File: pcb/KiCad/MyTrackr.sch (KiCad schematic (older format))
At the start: 36 parts, among them CN1 GPS_ANTENNA, CON1 MICRO_SD, P1 CONN_OLED, P2 CONN_ICSP, P3 CONN_01X05, P4 CONN_BAT, Q1 Q_PMOS_GSD, SW1 BTN_RESET, SW2 BTN_SEL, SW3 BTN_NEXT, SW4 BTN_PREV, SW5 BTN_BACK, U0 10A45B_Module, U1 ATMEGA48_88_168_328P-32SMD, U2 GPS-NEO-6M, U3 24AA32

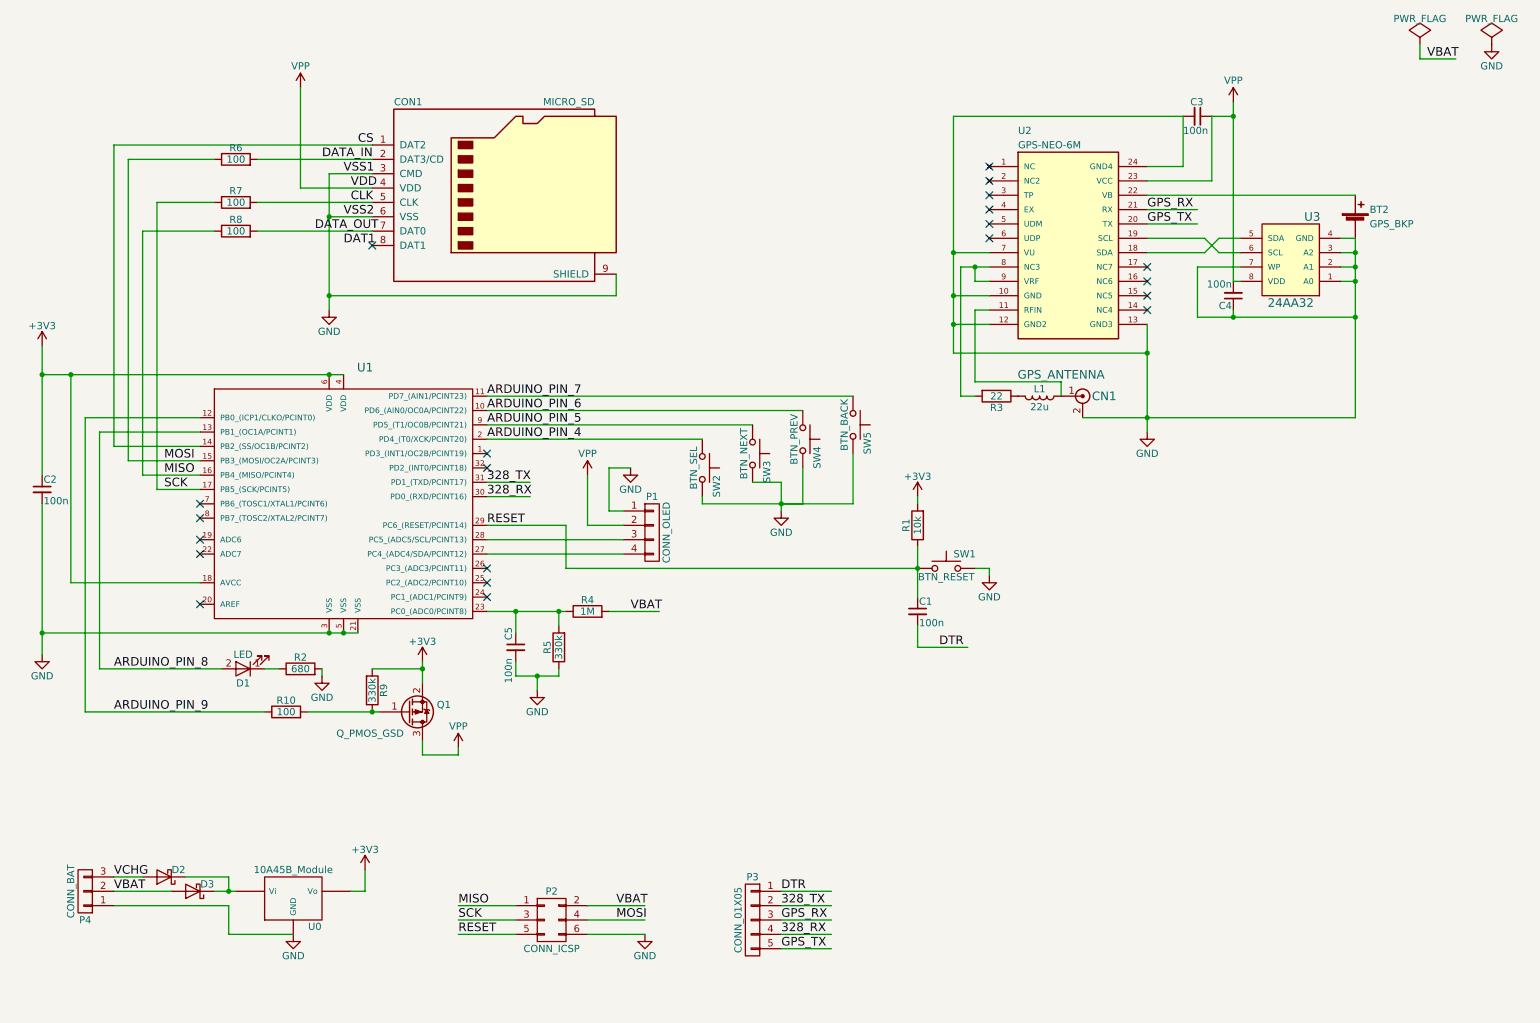
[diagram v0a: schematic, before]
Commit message: Corrections and tweaks after first prototype
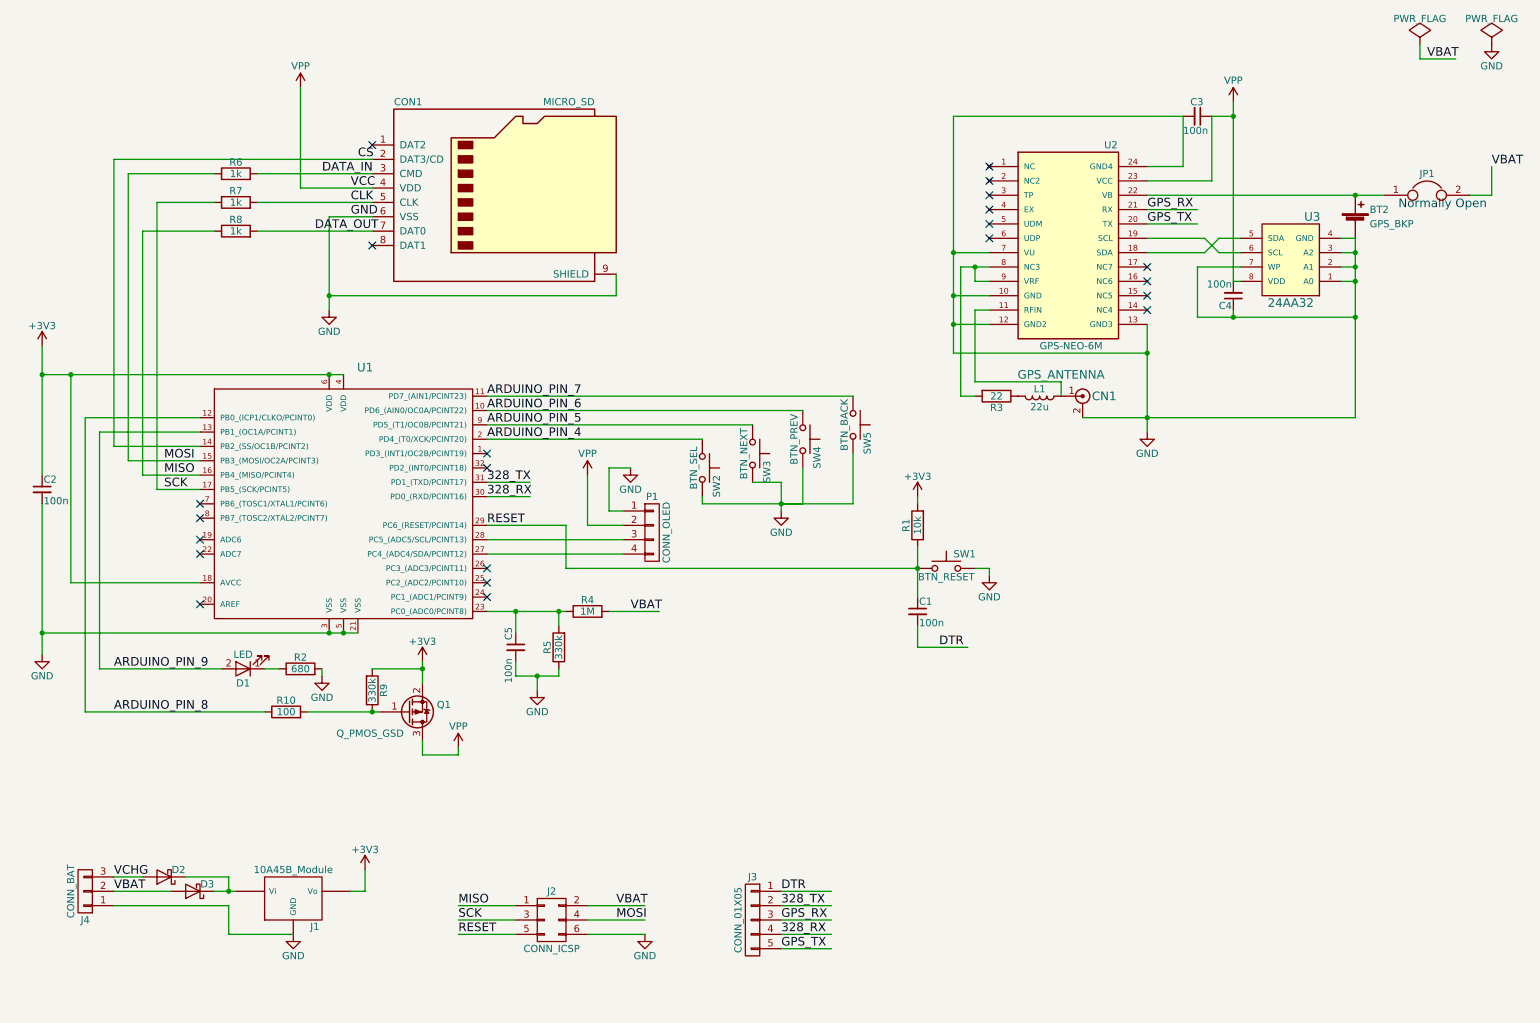
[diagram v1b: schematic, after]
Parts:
- added JP1: NO, Resistors_SMD:R_0805_HandSoldering, symbol Jumper
- R6, R7, R8: value 100 -> 1k
- U3: footprint SparkFun-Footprints:SF-SOIC-8 -> w_smd_dil:tssop-8
- renumbered U0 to J1, P2 to J2, P3 to J3, P4 to J4
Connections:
- net labels added: VCC
- net labels removed: DAT1, VDD, VSS1, VSS2
- wire segments 144 -> 145
- no-connect marks 21 -> 22
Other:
- note added: "Normally Open"
- moved on the sheet: R6

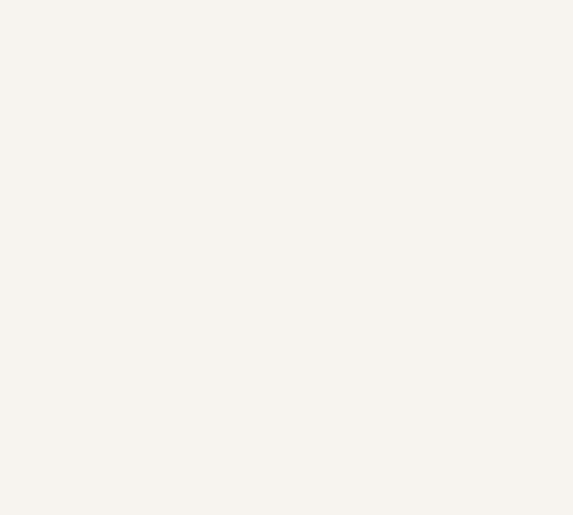
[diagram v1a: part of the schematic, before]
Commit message: Add screw holes, smooth corners and more
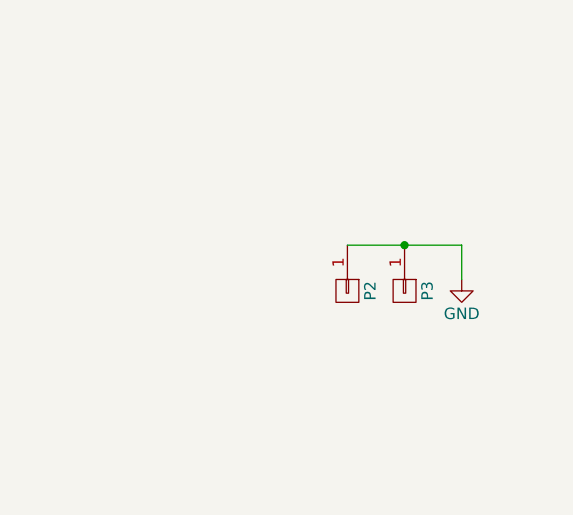
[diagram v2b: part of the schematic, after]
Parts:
- added P2, P3: CONN_01X01, Sukko:Screw_Hole_Plated_2mm, symbol CONN_01X01
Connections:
- wire segments 145 -> 147
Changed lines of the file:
@@
 Text Notes 10300 1950 0    60   ~ 0
 Normally Open
+$Comp
+L CONN_01X01 P2
+U 1 1 59B30D7B
+P 10300 6300
+F 0 "P2" H 10300 6400 50  0000 C CNN
+F 1 "CONN_01X01" V 10400 6300 50  0001 C CNN
+F 2 "Sukko:Screw_Hole_Plated_2mm" H 10300 6300 50  0001 C CNN
+F 3 "" H 10300 6300 50  0000 C CNN
+	1    10300 6300
+	0    1    1    0
+$EndComp
+$Comp
+L CONN_01X01 P3
+U 1 1 59B30E56
+P 10550 6300
+F 0 "P3" H 10550 6400 50  0000 C CNN
+F 1 "CONN_01X01" V 10650 6300 50  0001 C CNN
+F 2 "Sukko:Screw_Hole_Plated_2mm" H 10550 6300 50  0001 C CNN
+F 3 "" H 10550 6300 50  0000 C CNN
+	1    10550 6300
+	0    1    1    0
+$EndComp
+Wire Wire Line
+	10800 6100 10800 6250
+$Comp
+L GND #PWR022
+U 1 1 59B314E3
+P 10800 6250
+F 0 "#PWR022" H 10800 6000 50  0001 C CNN
+F 1 "GND" H 10800 6100 50  0000 C CNN
+F 2 "" H 10800 6250 50  0000 C CNN
+F 3 "" H 10800 6250 50  0000 C CNN
+	1    10800 6250
+	1    0    0    -1
+$EndComp
+Connection ~ 10550 6100
+Wire Wire Line
+	10300 6100 10800 6100
 $EndSCHEMATC

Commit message: Move project to KiCad 5.1.9, make all libs/footprints local
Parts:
- removed BT2: GPS_BKP, Battery_Holders:Keystone_3000_1x12mm-CoinCell, symbol Battery_Cell
- removed C1, C2, C3, C4, C5: 100n, Capacitors_SMD:C_0805_HandSoldering, symbol C_Small
- removed CON1: MICRO_SD, MicroSD GCT-MEM2055-00-190-01-A:GCT-MEM2055-00-190-01-A, symbol Micro_SD_Card
- removed D1: LED, LEDs:LED_0805, symbol LED
- removed D2, D3: D_Schottky, Diodes_SMD:SMA_Handsoldering, symbol D_Schottky
- removed J1: 10A45B_Module, Pin_Headers:Pin_Header_Straight_1x03, symbol 10A45B_Module
- removed J2: CONN_ICSP, Pin_Headers:Pin_Header_Straight_2x03, symbol CONN_02X03
- removed J3: CONN_01X05, Pin_Headers:Pin_Header_Straight_1x05, symbol CONN_01X05
- removed J4: CONN_BAT, Pin_Headers:Pin_Header_Straight_1x03, symbol CONN_01X03
- removed JP1: NO, Resistors_SMD:R_0805_HandSoldering, symbol Jumper
- removed L1: 22u, Resistors_SMD:R_0805_HandSoldering, symbol L
- removed P1: CONN_OLED, Pin_Headers:Pin_Header_Straight_1x04, symbol CONN_01X04
- removed P2, P3: CONN_01X01, Sukko:Screw_Hole_Plated_2mm, symbol CONN_01X01
- removed R1: 10k, Resistors_SMD:R_0805_HandSoldering, symbol R
- removed R10: 100, Resistors_SMD:R_0805_HandSoldering, symbol R
- removed R2: 680, Resistors_SMD:R_0805_HandSoldering, symbol R
- removed R3: 22, Resistors_SMD:R_0805_HandSoldering, symbol R
- removed R4: 1M, Resistors_SMD:R_0805_HandSoldering, symbol R
- removed R5, R9: 330k, Resistors_SMD:R_0805_HandSoldering, symbol R
- removed R6, R7, R8: 1k, Resistors_SMD:R_0805_HandSoldering, symbol R
- removed SW1: BTN_RESET, Buttons_Switches_SMD:SW_SPST_REED_CT05-XXXX-J1, symbol SW_Push
- removed SW2: BTN_SEL, MyKiCadLibs-Footprints:SW_TACT_SMD, symbol SW_Push
- removed SW3: BTN_NEXT, MyKiCadLibs-Footprints:SW_TACT_SMD, symbol SW_Push
- removed SW4: BTN_PREV, MyKiCadLibs-Footprints:SW_TACT_SMD, symbol SW_Push
- removed SW5: BTN_BACK, MyKiCadLibs-Footprints:SW_TACT_SMD, symbol SW_Push
- removed U2: GPS-NEO-6M, MOUDLE-GPS-NEO-6M_24P-16X12.2MM_:GPS24P-SMD-1.1-16X12.2MM, symbol GPS-NEO-6M
- added BT1: GPS_BKP, MyTrackr:BR1225A_KEYSTONE_1056, symbol Device:Battery_Cell
- added C1, C2, C3, C4, C5: 100n, Capacitor_SMD:C_0805_2012Metric_Pad1.18x1.45mm_HandSolder, symbol Device:C_Small
- added C6: CP1_Small, Capacitor_Tantalum_SMD:CP_EIA-7343-30_AVX-N_Pad2.25x2.55mm_HandSolder, symbol Device:CP1_Small
- added CON1: MICRO_SD, MyTrackr:GCT-MEM2055-00-190-01-A, symbol Connector:Micro_SD_Card_Det
- added D1: SS24, Diode_SMD:D_SMA, symbol Device:D_Schottky
- added H1, H2: MountingHole_Pad, MyTrackr:Screw_Hole_Plated_3mm, symbol Mechanical:MountingHole_Pad
- added J1: REGULATOR_3V3, Connector_PinHeader_2.54mm:PinHeader_1x03_P2.54mm_Vertical, symbol MyTrackr:10A45B_Module
- added J2: CONN_ICSP, Connector_PinHeader_2.54mm:PinHeader_2x03_P2.54mm_Vertical, symbol Connector_Generic:Conn_02x03_Odd_Even
- added J3: CONN_SERIAL, Connector_PinHeader_2.54mm:PinHeader_1x05_P2.54mm_Vertical, symbol Connector:Conn_01x05_Male
- added J4: CONN_BAT, Connector_PinHeader_2.54mm:PinHeader_1x03_P2.54mm_Vertical, symbol Connector:Conn_01x03_Male
- added JP1: JMP_BAT, Jumper:SolderJumper-2_P1.3mm_Open_TrianglePad1.0x1.5mm, symbol Jumper:Jumper_2_Open
- added L1: 22, Resistor_SMD:R_0805_2012Metric_Pad1.20x1.40mm_HandSolder, symbol Device:L
- added LD1: LED, LED_SMD:LED_0805_2012Metric_Pad1.15x1.40mm_HandSolder, symbol Device:LED
- added P1: CONN_OLED, Connector_PinHeader_2.54mm:PinHeader_1x04_P2.54mm_Vertical, symbol Connector:Conn_01x04_Male
- added R1: 10k, Resistor_SMD:R_0805_2012Metric_Pad1.20x1.40mm_HandSolder, symbol Device:R
- added R10: 100, Resistor_SMD:R_0805_2012Metric_Pad1.20x1.40mm_HandSolder, symbol Device:R
- added R2: 680, Resistor_SMD:R_0805_2012Metric_Pad1.20x1.40mm_HandSolder, symbol Device:R
- added R3: 22, Resistor_SMD:R_0805_2012Metric_Pad1.20x1.40mm_HandSolder, symbol Device:R
- added R4: 1M, Resistor_SMD:R_0805_2012Metric_Pad1.20x1.40mm_HandSolder, symbol Device:R
- added R5, R9: 330k, Resistor_SMD:R_0805_2012Metric_Pad1.20x1.40mm_HandSolder, symbol Device:R
- added R6, R7, R8: 1k, Resistor_SMD:R_0805_2012Metric_Pad1.20x1.40mm_HandSolder, symbol Device:R
- added SW1: BTN_RESET, Button_Switch_SMD:SW_SPST_REED_CT05-XXXX-J1, symbol Switch:SW_Push
- added SW2: BTN_SEL, Button_Switch_SMD:SW_SPST_EVPBF, symbol Switch:SW_Push
- added SW3: BTN_NEXT, Button_Switch_SMD:SW_SPST_EVPBF, symbol Switch:SW_Push
- added SW4: BTN_PREV, Button_Switch_SMD:SW_SPST_EVPBF, symbol Switch:SW_Push
- added SW5: BTN_BACK, Button_Switch_SMD:SW_SPST_EVPBF, symbol Switch:SW_Push
- added U2: GPS-NEO-6M, MyTrackr:GPS24P-SMD-1.1-16X12.2MM, symbol MOUDLE-GPS-NEO-6M_24P-16X12.2MM_:MOUDLE-GPS-NEO-6M(24P-16X12.2MM)
- added V0: OSHW_LOGO, Symbol:OSHW-Logo_5.7x6mm_Copper, symbol void:Void
- CN1: footprint MyKiCadLibs-Footprints:CONN-RF-UFL -> MyTrackr:CONN-RF-UFL; symbol COAX -> MyTrackr-rescue:COAX
- Q1: footprint TO_SOT_Packages_SMD:SOT-23_Handsoldering -> Package_TO_SOT_SMD:SOT-23; symbol Q_PMOS_GSD -> MyTrackr-rescue:Q_PMOS_GSD
- U1: footprint Housings_QFP:LQFP-32_7x7mm_Pitch0.8mm -> Package_QFP:TQFP-32_7x7mm_P0.8mm; symbol ATMEGA48_88_168_328P-32SMD -> MyTrackr-rescue:ATMEGA48_88_168_328P-32SMD
- U3: symbol 24AA32 -> MyTrackr-rescue:24AA32
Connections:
- net labels added: CARD_DETECT
- wire segments 147 -> 186
- no-connect marks 22 -> 19
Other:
- note added: "IDEAL: 200 mA, 2.7 kohm @100Mhz\n(Thanks astrobeed)"
- note added: "Short to use main battery\nfor GPS backup as well"
- note removed: "Normally Open"

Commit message: Remove old cruft
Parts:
- removed CN1: GPS_ANTENNA, MyTrackr:CONN-RF-UFL, symbol MyTrackr-rescue:COAX
- removed Q1: Q_PMOS_GSD, Package_TO_SOT_SMD:SOT-23, symbol MyTrackr-rescue:Q_PMOS_GSD
- removed U1: ATMEGA48_88_168_328P-32SMD, Package_QFP:TQFP-32_7x7mm_P0.8mm, symbol MyTrackr-rescue:ATMEGA48_88_168_328P-32SMD
- removed U3: 24AA32, w_smd_dil:tssop-8, symbol MyTrackr-rescue:24AA32
- added CN1: GPS_ANTENNA, MyTrackr:CONN-RF-UFL, symbol Connector:Conn_Coaxial
- added Q1: Q_PMOS_GSD, Package_TO_SOT_SMD:SOT-23, symbol Device:Q_PMOS_GSD
- added U1: ATMEGA328PA, Package_QFP:TQFP-32_7x7mm_P0.8mm, symbol atmega328:ATMEGA48_88_168_328P-32SMD
- added U3: 24AA32, w_smd_dil:tssop-8, symbol 24aa32:24AA32
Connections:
- net +3V3: now also Q1.2 (S), U1.18 (AVCC), U1.4 (VDD), U1.6 (VDD)
- net 328_RX: now also U1.30 (PD0_(RXD/PCINT16))
- net 328_TX: now also U1.31 (PD1_(TXD/PCINT17))
- net ARDUINO_PIN_4: now also U1.2 (PD4_(T0/XCK/PCINT20))
- net ARDUINO_PIN_5: now also U1.9 (PD5_(T1/OC0B/PCINT21))
- net ARDUINO_PIN_6: now also U1.10 (PD6_(AIN0/OC0A/PCINT22))
- net ARDUINO_PIN_7: now also U1.11 (PD7_(AIN1/PCINT23))
- net ARDUINO_PIN_8: now also U1.12 (PB0_(ICP1/CLKO/PCINT0))
- net ARDUINO_PIN_9: now also U1.13 (PB1_(OC1A/PCINT1))
- net CARD_DETECT: now also U1.32 (PD2_(INT0/PCINT18))
- net CS: now also U1.14 (PB2_(SS/OC1B/PCINT2))
- net GND: now also CN1.2 (Ext), U1.3 (VSS), U3.1 (A0), U3.2 (A1), U3.3 (A2), U3.4 (GND), U3.7 (WP)
- net MISO: now also U1.16 (PB4_(MISO/PCINT4))
- net MOSI: now also U1.15 (PB3_(MOSI/OC2A/PCINT3))
- net RESET: now also U1.29 (PC6_(RESET/PCINT14))
- net SCK: now also U1.17 (PB5_(SCK/PCINT5))
- net VPP: now also Q1.3 (D), U3.8 (VDD)
- net at L1.1, U2.11 (RFIN): now also CN1.1 (In)
- net at U2.18 (SDA): now also U3.5 (SDA)
- net at U2.19 (SCL): now also U3.6 (SCL)
- net at C5.1, R4.2, R5.1: now also U1.23 (PC0_(ADC0/PCINT8))
- net at P1.4 (Pin_4): now also U1.27 (PC4_(ADC4/SDA/PCINT12))
- net at P1.3 (Pin_3): now also U1.28 (PC5_(ADC5/SCL/PCINT13))
- net at R10.1, R9.2: now also Q1.1 (G)

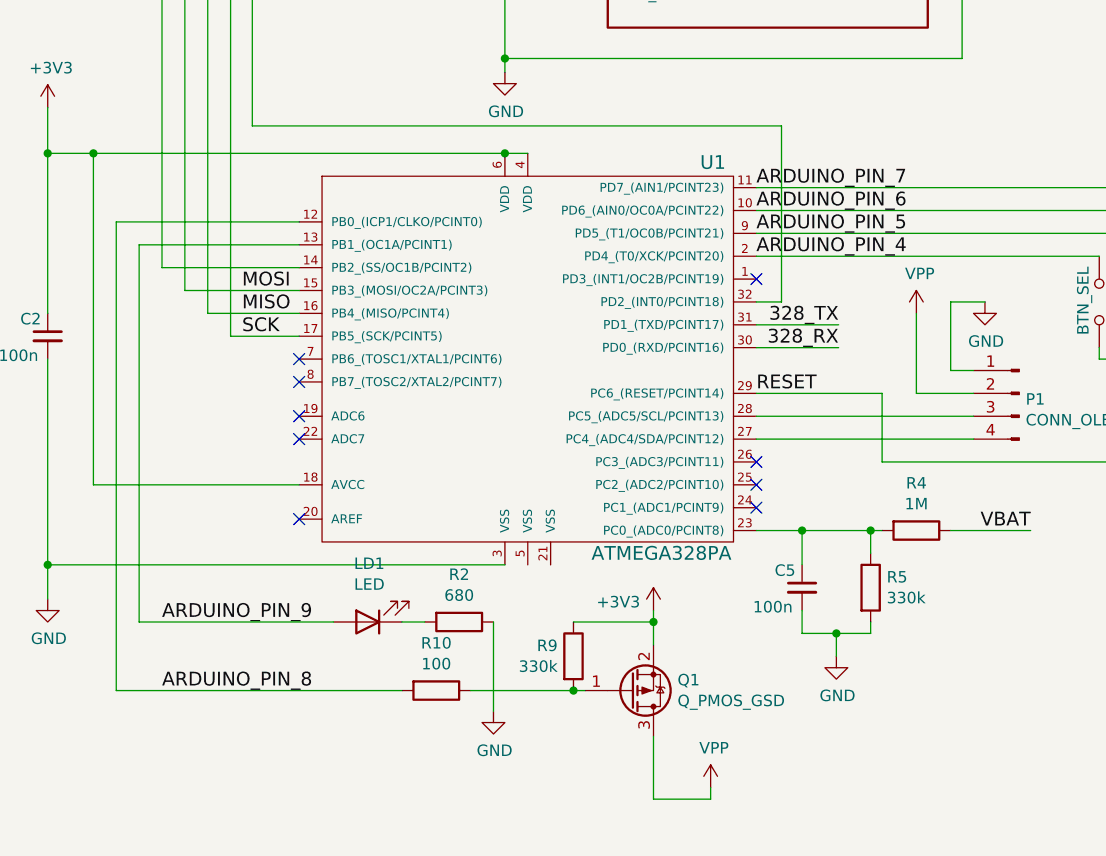
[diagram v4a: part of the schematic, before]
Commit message: Connect all grounds, use meaningful signal names
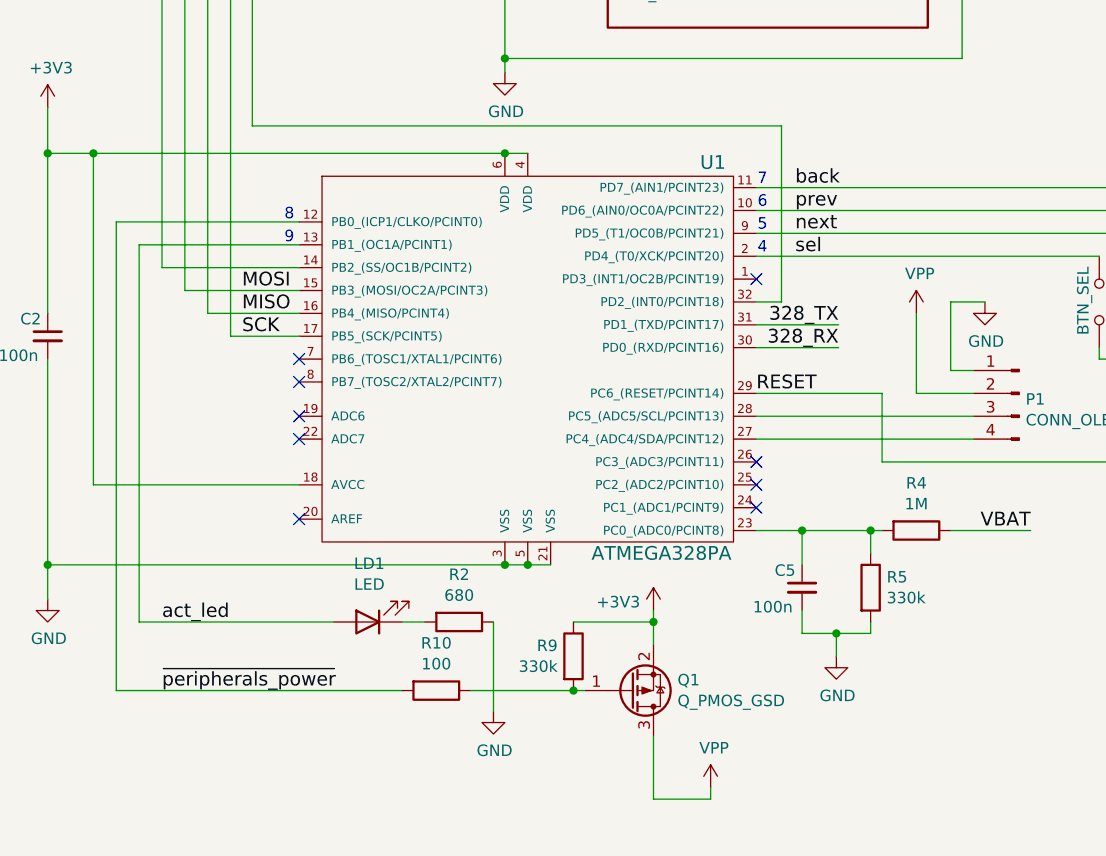
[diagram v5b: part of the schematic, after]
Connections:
- net GND: now also U1.21 (VSS), U1.5 (VSS)
- net ARDUINO_PIN_4 renamed sel
- net ARDUINO_PIN_5 renamed next
- net ARDUINO_PIN_6 renamed prev
- net ARDUINO_PIN_7 renamed back
- net ARDUINO_PIN_8 renamed ~peripherals_power
- net ARDUINO_PIN_9 renamed act_led
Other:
- note added: "4"
- note added: "5"
- note added: "6"
- note added: "7"
- note added: "8"
- note added: "9"
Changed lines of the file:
@@
 Comment4 "Work in progress!"
 $EndDescr
-Text Label 3950 3550 0    60   ~ 0
-ARDUINO_PIN_4
-Text Label 3950 3450 0    60   ~ 0
-ARDUINO_PIN_5
-Text Label 3950 3350 0    60   ~ 0
-ARDUINO_PIN_6
-Text Label 3950 3250 0    60   ~ 0
-ARDUINO_PIN_7
+Text Label 4120 3550 0    60   ~ 0
+sel
+Text Label 4120 3450 0    60   ~ 0
+next
+Text Label 4120 3350 0    60   ~ 0
+prev
+Text Label 4120 3250 0    60   ~ 0
+back
 NoConn ~ 8550 2350
 NoConn ~ 8550 2450
@@
 DTR
 Text Label 1350 5150 0    60   ~ 0
-ARDUINO_PIN_9
+act_led
 Text Label 1700 3700 0    60   ~ 0
 MOSI
@@
 NoConn ~ 3950 3650
 Text Label 1350 5450 0    60   ~ 0
-ARDUINO_PIN_8
+~peripherals_power
 Text Label 1350 6600 0    60   ~ 0
 VCHG
@@
 	2850 3100 2950 3100
 Connection ~ 2850 3100
+Wire Wire Line
+	2850 4900 2950 4900
+Connection ~ 2850 4900
+Connection ~ 2950 4900
+Wire Wire Line
+	2950 4900 3050 4900
+Text Notes 3955 3245 0    50   ~ 0
+7
+Text Notes 3955 3345 0    50   ~ 0
+6
+Text Notes 3955 3445 0    50   ~ 0
+5
+Text Notes 3955 3545 0    50   ~ 0
+4
+Text Notes 1885 3500 0    50   ~ 0
+9
+Text Notes 1885 3400 0    50   ~ 0
+8
 $EndSCHEMATC
